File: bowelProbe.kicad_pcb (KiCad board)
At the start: 4 copper layers, 84.7 x 41.9 mm, 94 parts, among them J1 Conn_01x01, J12 Conn_01x01, J13 Conn_01x01, J2 Conn_01x01, J3 Conn_01x08, J4 Conn_01x08, U1 L7805CV, U2 LT8330, U3 ATmega328P, U4 AD9833BRMZ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

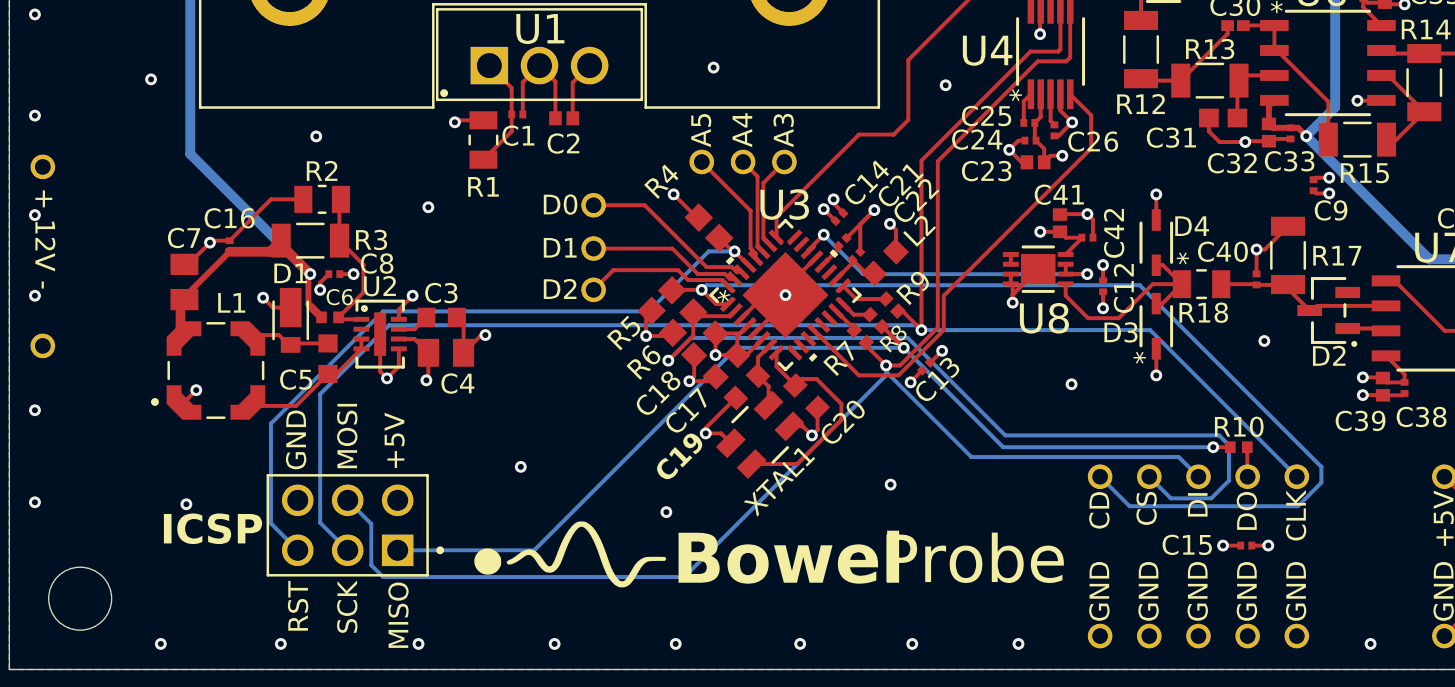
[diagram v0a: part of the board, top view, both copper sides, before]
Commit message: Part Replacement
Replaced Coilcraft inductor for an in stock part. Adjusted PCBA files accordingly.
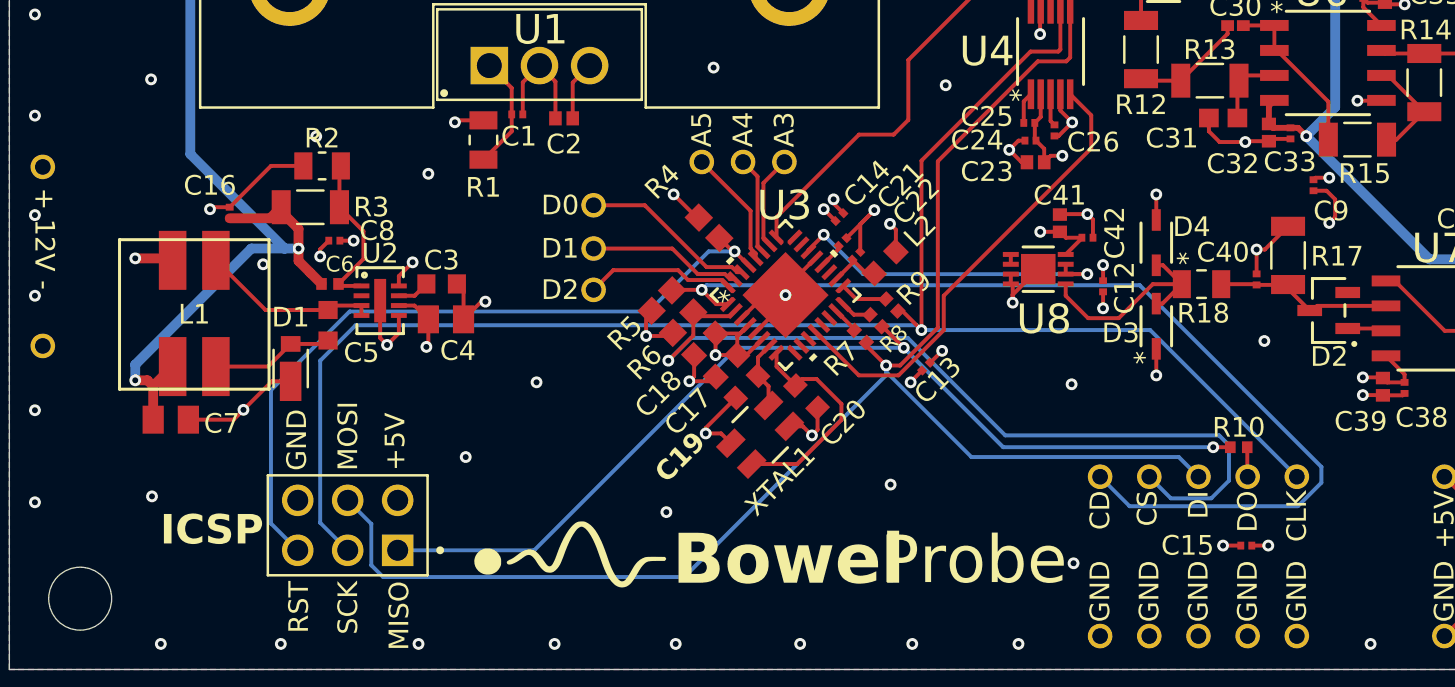
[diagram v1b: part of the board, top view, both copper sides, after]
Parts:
- L1: value LPD5030-472MRC -> SRF0703-4R7M; footprint BowelProbe:InductorCoupled -> BowelProbe:Inductor4.7uReplacement
- moved C7 7.03 mm to (69.4, 74.8), turned to 180 degrees
- moved L1 3.05 mm to (70.6, 69.5), turned to 0 degrees
- moved D1 2.45 mm to (75.5, 72.2), turned to 90 degrees
- moved C16 1.70 mm to (72.4, 64.3)
- moved C3 1.70 mm to (83.2, 67.9)
- moved C4 1.70 mm to (83.4, 69.7)
- moved C5 1.70 mm to (77.4, 70.0), turned to 90 degrees
- moved C6 1.70 mm to (77.5, 67.9)
- moved C8 1.70 mm to (77.7, 65.7)
- moved R2 1.70 mm to (77.1, 61.9)
- moved R3 1.70 mm to (76.5, 64.0)
- moved U2 1.70 mm to (80.0, 68.8)
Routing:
- net /-12V: track 125.0 -> 133.7 mm, vias 3 -> 4
- net GND: track 90.3 -> 94.7 mm, vias 79 -> 82
- net Net-(C5-Pad1): track 4.14 -> 6.25 mm
- net Net-(C5-Pad2): track 7.30 -> 9.04 mm
- net /SCK: track 84.5 -> 85.5 mm
- net /nReset: track 36.3 -> 37.3 mm
- net /+12V: track 18.0 -> 18.8 mm

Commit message: Part Replacements
Replaced crystal and schottky diode. Adjusted schematic, PCB, and BOM accordingly. Organized schematic and colored different sections.
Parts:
- D1: value SchottkyDiode -> PMEG6010CEJ,115; footprint BowelProbe:SchottkyDiode -> BowelProbe:SchottkyReplacement
- moved C7 10.8 mm to (67.4, 64.2), turned to -90 degrees
- moved L1 0.60 mm to (70.2, 69.9), turned to 90 degrees
- moved D1 0.32 mm to (75.6, 71.9)
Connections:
- L1 pad 2: Net-(C5-Pad2) -> /-12V
- L1 pad 3: Net-(C5-Pad1) -> Net-(C5-Pad2)
- L1 pad 4: /-12V -> Net-(C5-Pad1)
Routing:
- net /-12V: track 133.7 -> 131.5 mm
- net Net-(C5-Pad2): track 9.04 -> 7.02 mm
- net Net-(C5-Pad1): track 6.25 -> 4.64 mm
- net GND: track 94.7 -> 93.9 mm

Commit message: Fully Reviewed and Cleared For Immediate Order
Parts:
- D1: value PMEG6010CEJ,115 -> SchottkyDiode
- U8: value MCP6002-E/MC -> MCP6002T-E/MC
- XTAL1: value TSX-3225 16.0000MF09Z-AC3 -> TSX-3225 16.0000MF18X-AC3
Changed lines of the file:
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@@
 			)
 		)
-		(property "Value" "PMEG6010CEJ,115"
+		(property "Value" "SchottkyDiode"
 			(at 0 0 90)
 			(layer "F.Fab")
@@
 			)
 		)
-		(property "Datasheet" "https://assets.nexperia.com/documents/data-sheet/PMEG6010CEJ.pdf"
+		(property "Datasheet" "https://diotec.com/request/datasheet/sdb160ws.pdf"
 			(at 0 0 90)
 			(layer "F.Fab")
@@
 			)
 		)
-		(property "Description" "1 Independent 10A 1A 50uA@60V 60V 660mV@1A SOD-323F Schottky Diodes ROHS "
+		(property "Description" "1 Independent 10A 1A 50uA@60V 60V 660mV@1A SOD-323F Schottky Diodes ROHS"
 			(at 0 0 90)
 			(layer "F.Fab")
@@
 			)
 		)
-		(property "MF" "Nexperia"
+		(property "MF" "Diotec Semiconductor"
 			(at 0 0 90)
 			(unlocked yes)
@@
 			)
 		)
-		(property "MP" ""
+		(property "MP" "SDB160WS-AQ"
 			(at 0 0 90)
 			(unlocked yes)
@@
 			)
 		)
-		(property "Manufacturer Product Number" "PMEG6010CEJ,115"
+		(property "Manufacturer Product Number" "SDB160WS-AQ"
 			(at 0 0 90)
 			(unlocked yes)
@@
 			)
 		)
-		(property "Value" "MCP6002-E/MC"
+		(property "Value" "MCP6002T-E/MC"
 			(at 0 0 0)
 			(unlocked yes)
@@
 			)
 		)
-		(property "Description" "-40℃~+125℃ 1.8V~6V 100uA 1MHz 1pA 1pA 2 23mA 28nV/√Hz@1kHz 2uV/℃ 4.5mV 600V/ms 6V 76dB Rail-to-Rail Input, Rail-to-Rail Output DFN-8(2x3) Operational Amplifier ROHS"
+		(property "Description" "-40℃~+125℃ 1.8V~6V 100uA 1MHz 1pA 1pA 2 23mA 28nV/√Hz@1kHz 2uV/℃ 4.5mV 600V/ms 6V 76dB Rail-to-Rail Input, Rail-to-Rail Output DFN-8-EP(2x3) Operational Amplifier ROHS"
 			(at 0 0 0)
 			(layer "F.Fab")
@@
 			)
 		)
-		(property "LCSC PN" "C185041"
+		(property "LCSC PN" "C623660"
 			(at 0 0 0)
 			(unlocked yes)
@@
 			)
 		)
-		(property "Value" "TSX-3225 16.0000MF09Z-AC3"
+		(property "Value" "TSX-3225 16.0000MF18X-AC3"
 			(at 0 0 225)
 			(unlocked yes)
@@
 			)
 		)
-		(property "Description" "-20℃~+75℃ 16MHz 60Ω 9pF ±10ppm ±9ppm SMD3225-4P Crystals ROHS"
+		(property "Description" "-40℃~+85℃ 16MHz 60Ω 9pF ±10ppm ±18ppm SMD3225-4P Crystals ROHS"
 			(at 0 0 45)
 			(layer "F.Fab")
@@
 			)
 		)
-		(property "Manufacturer Product Number" "TSX-3225 16.0000MF09Z-AC3"
+		(property "Manufacturer Product Number" "TSX-3225 16.0000MF18X-AC3"
 			(at 0 0 225)
 			(unlocked yes)
@@
 			)
 		)
-		(property "LCSC PN" "C2650454"
+		(property "LCSC PN" "C1986974"
 			(at 0 0 225)
 			(unlocked yes)
@@
 		)
 		(fp_line
-			(start -3.8 -3.8)
+			(start 2.5 -3.8)
 			(end 3.8 -3.8)
 			(stroke
@@
 		(fp_line
 			(start -3.8 -3.8)
+			(end -2.5 -3.8)
+			(stroke
+				(width 0.1524)
+				(type solid)
+			)
+			(layer "F.SilkS")
+		)
+		(fp_line
+			(start -3.8 -3.8)
 			(end -3.8 3.8)
 			(stroke
@@
 		)
 		(fp_line
-			(start -3.8 3.8)
+			(start 2.5 3.8)
 			(end 3.8 3.8)
 			(stroke
 				(width 0.1524)
+				(type solid)
+			)
+			(layer "F.SilkS")
+		)
+		(fp_line
+			(start -3.8 3.8)
+			(end -2.5 3.8)
+			(stroke
+				(width 0.1524)

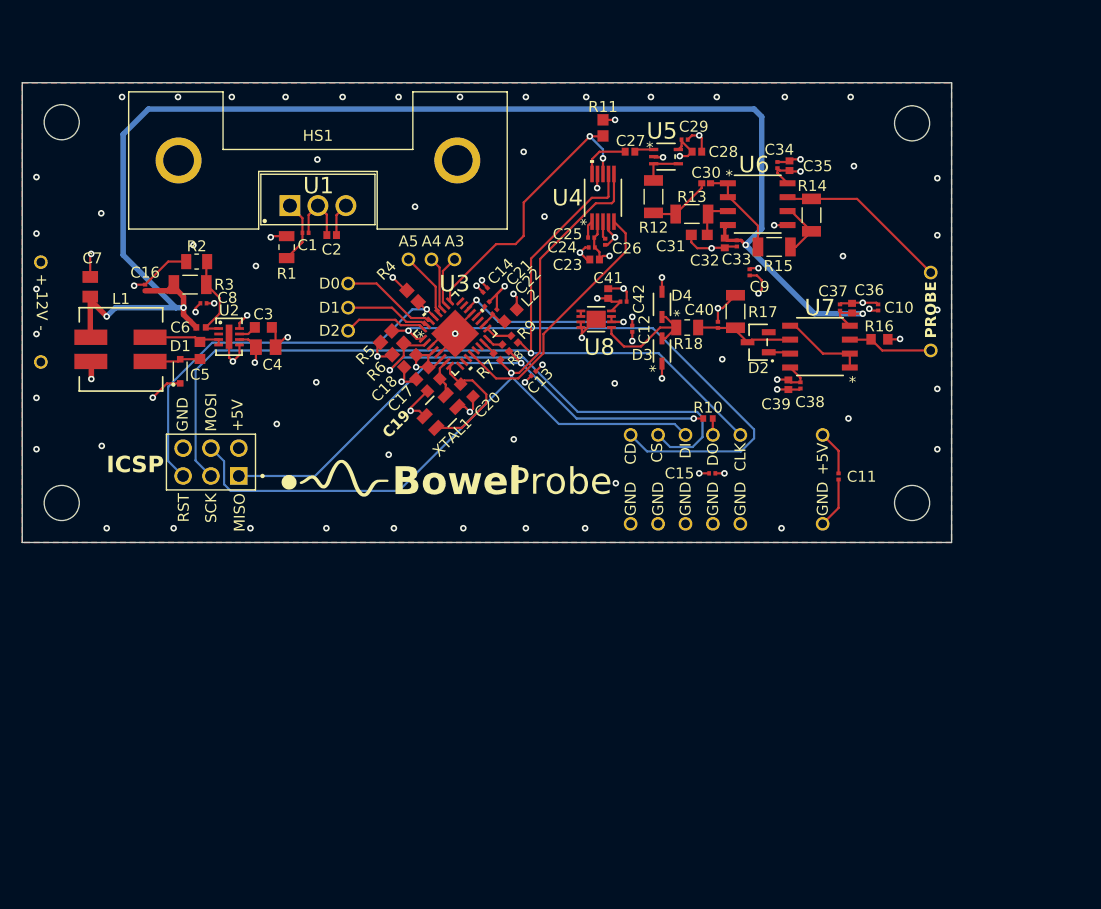
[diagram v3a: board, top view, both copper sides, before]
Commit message: Rev 1 Progress
- Updated BOM for the SMT +12V and +5V regulators

- Removed tracks from previous board

- Deleted heatsink and +5V THT regulator from layout

- Set an initial layout plan (~80% complete)

- Updated various silkscreens to signal the proper part and orientation

- Updated silkscreen for Vin, I2C, and UART pins
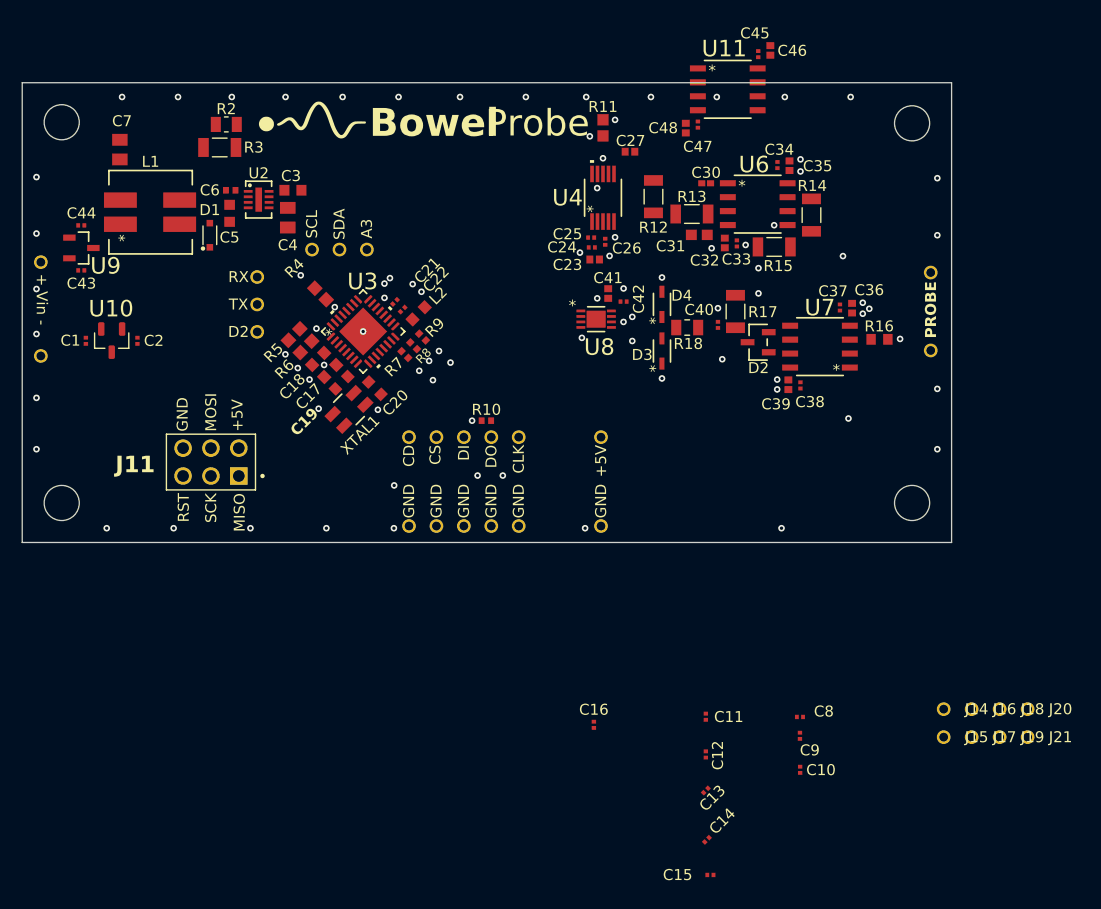
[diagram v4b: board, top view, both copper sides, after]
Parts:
- removed C28: 10u, BowelProbe:Cap10uF
- removed C29: 0.1u, BowelProbe:Cap0.1uF
- removed HS1: Heatsink, BowelProbe:Heatsink
- removed R1: 1k, BowelProbe:Resistor1k
- removed U1: L7805CV, BowelProbe:L7805CV
- removed U5: Buffer, BowelProbe:Buffer
- added C43: 0.1u, BowelProbe:Cap0.1uF, F.Cu at (66.6, 62.7)
- added C44: 0.1u, BowelProbe:Cap0.1uF, F.Cu at (66.6, 58.6)
- added C45: 0.1u, BowelProbe:Cap0.1uF, F.Cu at (128.3, 43.0)
- added C46: 10u, BowelProbe:Cap10uF, F.Cu at (129.4, 42.7)
- added C47: 0.1u, BowelProbe:Cap0.1uF, F.Cu at (122.8, 49.4)
- added C48: 10u, BowelProbe:Cap10uF, F.Cu at (121.7, 49.7)
- added J14: Conn_01x01, BowelProbe:CT3149-2, F.Cu at (145.2, 102.7)
- added J15: Conn_01x01, BowelProbe:CT3149-2, F.Cu at (145.2, 105.2)
- added J16: Conn_01x01, BowelProbe:CT3149-2, F.Cu at (147.7, 102.7)
- added J17: Conn_01x01, BowelProbe:CT3149-2, F.Cu at (147.7, 105.2)
- added J18: Conn_01x01, BowelProbe:CT3149-2, F.Cu at (150.3, 102.7)
- added J19: Conn_01x01, BowelProbe:CT3149-2, F.Cu at (150.3, 105.2)
- added J20: Conn_01x01, BowelProbe:CT3149-2, F.Cu at (152.8, 102.7)
- added J21: Conn_01x01, BowelProbe:CT3149-2, F.Cu at (152.8, 105.2)
- added U10: TLV76050DBZR, BowelProbe:TLV76050DBZR, F.Cu at (69.4, 69.1)
- added U11: TL072ACDR, BowelProbe:TL072smd, F.Cu at (125.5, 46.2)
- added U9: LM3480IM3-12/NOPB, BowelProbe:LM3480IM3-12_NOPB, F.Cu at (66.6, 60.7)
- C2: value 10u -> 0.1u; footprint BowelProbe:Cap10uF -> BowelProbe:Cap0.1uF
- moved C8 66.2 mm to (132.1, 103.4)
- moved C16 57.1 mm to (113.3, 104.1)
- moved C14 54.0 mm to (123.6, 114.6)
- moved C10 42.7 mm to (132.1, 108.2)
- moved C9 42.5 mm to (132.1, 105.1)
- moved C13 41.1 mm to (123.5, 110.1)
- moved C12 39.4 mm to (123.5, 106.8)
- moved C15 36.6 mm to (123.9, 117.8)
- moved G*** 32.7 mm to (87.7, 49.5)
- moved C11 25.0 mm to (123.5, 103.4)
- moved C1 22.3 mm to (67.0, 69.1), turned to -90 degrees
- moved J3 20.2 mm to (105.2, 77.9)
- moved J4 20.2 mm to (105.2, 86.0)
- moved R10 20.2 mm to (103.5, 76.4)
- moved C2 20.2 mm to (71.7, 69.1), turned to -90 degrees
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- renumbered ICSP to J11, D0 to RX, A5 to SCL, A4 to SDA, D1 to TX
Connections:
- net /A4 renamed /SDA
- net /A5 renamed /SCL
- net /D0 renamed /RX
- net /D1 renamed /TX
- C1 pad 1: Net-(U1-INPUT) -> /Vin
- J12 pad 1: /Vamplified -> /Vampbuf
- J2 pad 1: /+12V -> /Vin
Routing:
- net /-12V: track 131.5 -> 0.00 mm, vias 4 -> 2
- net GND: track 93.9 -> 0.00 mm, vias 82 -> 57
- net /SCK: track 85.5 -> 0.00 mm
- net /MOSI: track 78.2 -> 0.00 mm
- net /CD: track 51.7 -> 0.00 mm
- net /MISO: track 50.2 -> 0.00 mm
- net /nSS: track 43.2 -> 0.00 mm
- net /+5V: track 38.7 -> 0.00 mm, vias 13 -> 12
- net /nReset: track 37.3 -> 0.00 mm
- net /nSS_Sin: track 26.5 -> 0.00 mm
- net /CLKO: track 23.9 -> 0.00 mm
- net /+12V: track 18.5 -> 0.00 mm, vias 9 -> 4
- net /VADC: track 17.0 -> 0.00 mm
- net /Vamplified: track 15.9 -> 0.00 mm
- net Net-(U3-PB7): track 11.4 -> 0.00 mm
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- removed copper zone on In2.Cu, net /+12V
- removed copper zone on In2.Cu, net /+5V
- removed copper zone on B.Cu, net GND
- removed copper zone on F.Cu, net GND
- removed copper zone on In1.Cu, net GND
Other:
- board text added: "+ Vin -"
- board text removed: "+ 12V -"

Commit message: Initial Layout (Rev 1)
Initial layout plan nearly complete. Needs positioning of test points and stitching capacitors as well as any additional vias afterwards. Also considering making available more ATMega channels as space allows after placement and routing.
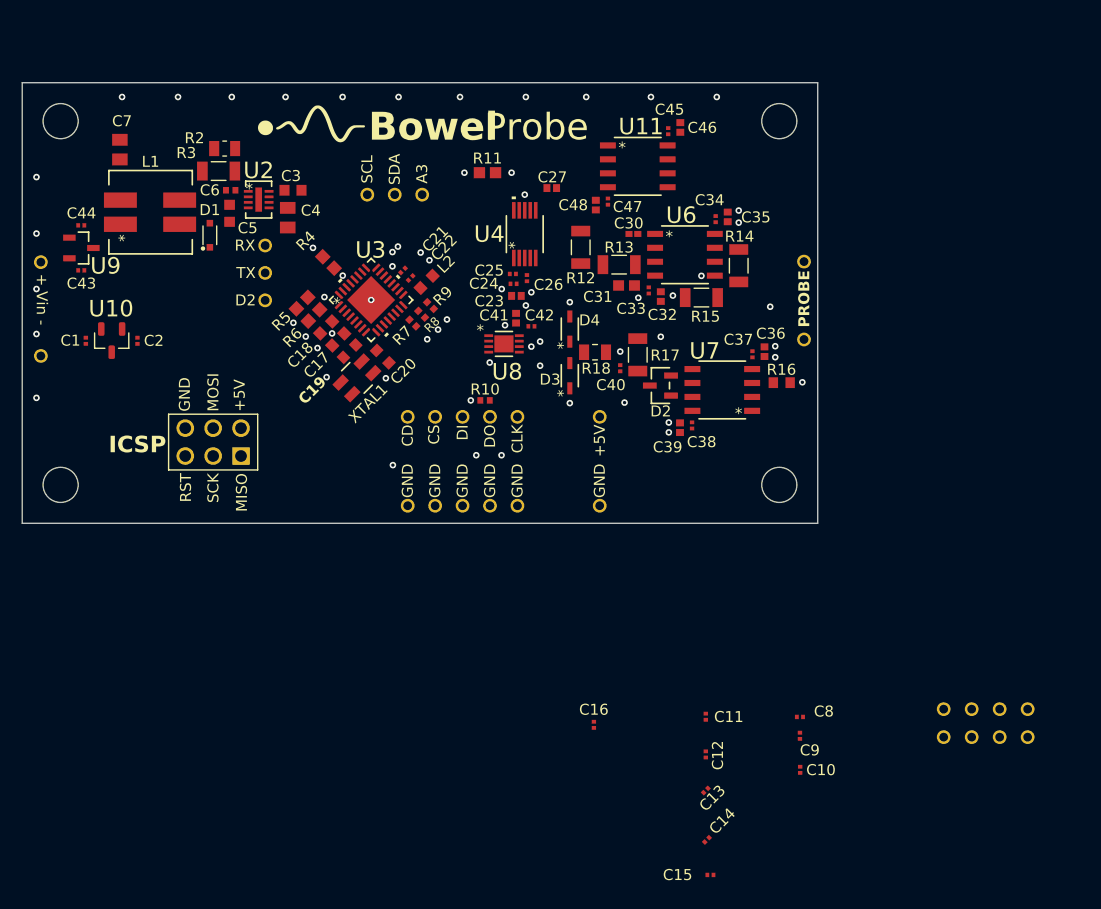
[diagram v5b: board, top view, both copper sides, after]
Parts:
- moved REF** 12.2 mm to (130.2, 82.2)
- moved REF** 12.1 mm to (130.2, 49.1)
- moved J12 11.6 mm to (132.4, 61.9)
- moved J13 11.6 mm to (132.4, 69.0)
- moved R11 11.3 mm to (103.6, 53.8), turned to 180 degrees
- moved C48 10.8 mm to (113.5, 56.8)
- moved U11 10.8 mm to (117.3, 53.2)
- moved C45 10.8 mm to (120.1, 50.0)
- moved C46 10.8 mm to (121.2, 49.7)
- moved C47 10.8 mm to (114.6, 56.4)
- moved C39 10.6 mm to (121.2, 77.0)
- moved C38 10.5 mm to (122.2, 76.8)
- moved R16 9.74 mm to (130.4, 72.9)
- moved C40 9.74 mm to (115.7, 71.6)
- moved D2 9.74 mm to (119.4, 73.2)
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- renumbered J11 to ICSP
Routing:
- net GND: vias 57 -> 39
- net /+5V: vias 12 -> 11
- net /+12V: vias 4 -> 2
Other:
- board size 84.7 x 41.9 mm -> 72.5 x 40.1 mm
